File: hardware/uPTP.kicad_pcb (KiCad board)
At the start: 4 copper layers, 40 x 50 mm, 78 parts, among them J1 PPS_UFL, J2 PPS_SMA, J3 LED, J4 UART_HDR, J5 HC-RJ45-055-7, J6 AUX_PWR, J7 PROG, U1 XC6206P332MR-G, U2 SI3404-A-GMR, U3 CH32V307WCU6, X1 X50328MSB2GI

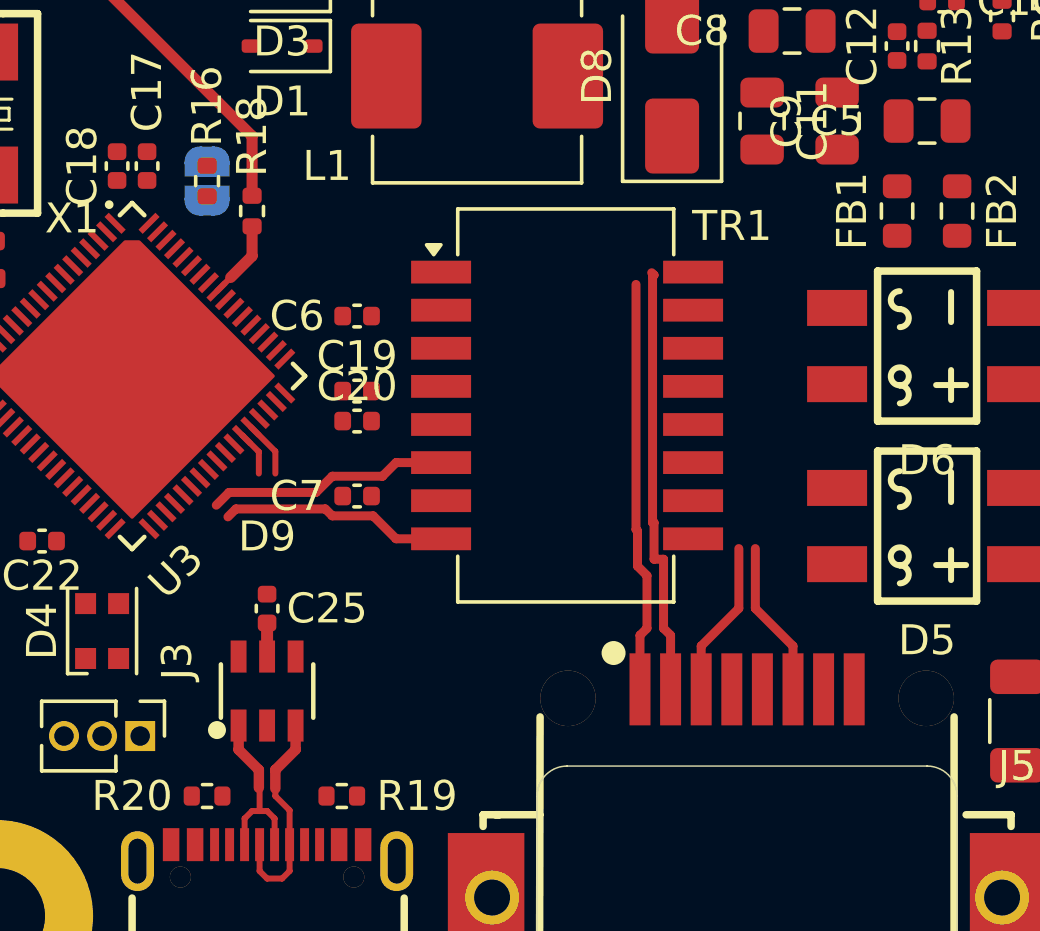
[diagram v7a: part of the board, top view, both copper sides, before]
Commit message: Change pin layout to make Ethernet Routing nicer
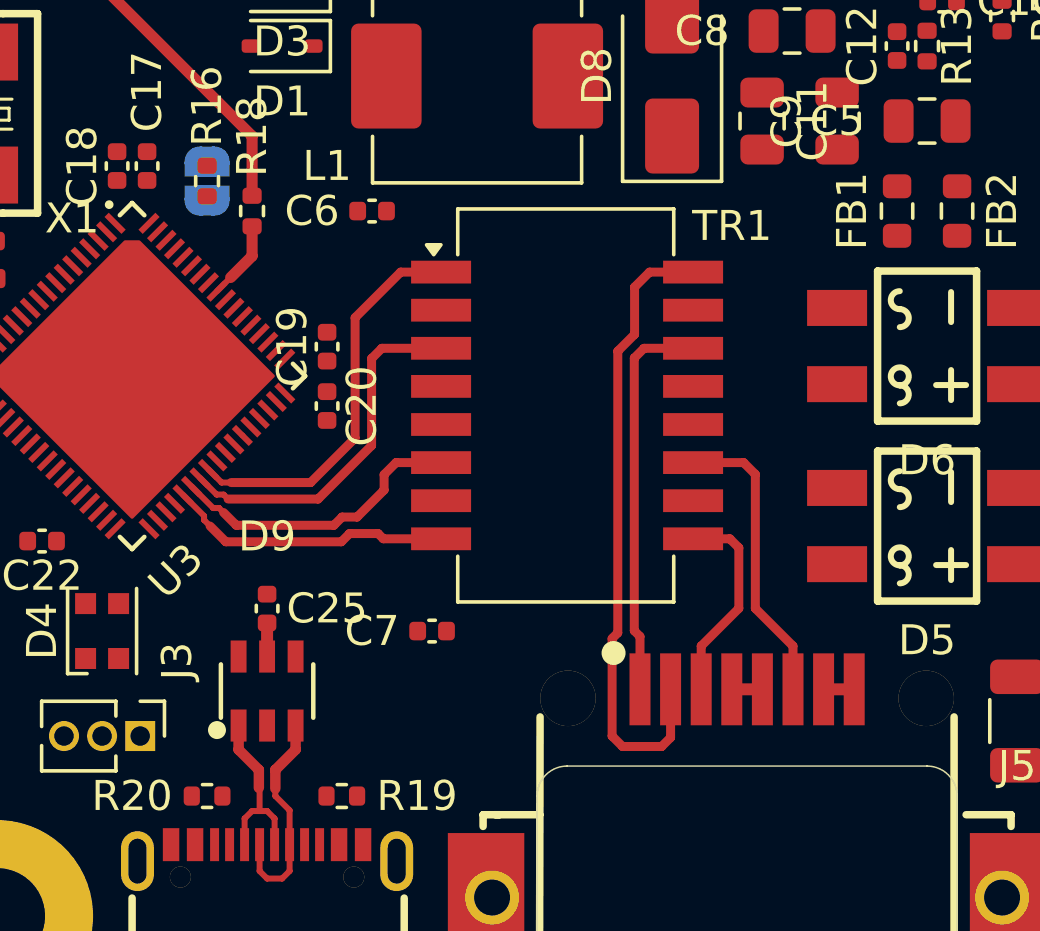
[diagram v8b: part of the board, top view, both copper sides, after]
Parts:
- moved C7 5.15 mm to (148.5, 111.5)
- moved C6 3.54 mm to (146.5, 97.5)
- moved C19 1.79 mm to (145.0, 102.0), turned to 90 degrees
- moved C20 1.12 mm to (145.0, 104.0), turned to -90 degrees
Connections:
- TR1 pad 1: /Ethernet and POE/ETH_D_TX_P -> /Ethernet and POE/ETH_D_TX_N
- TR1 pad 11: /Ethernet and POE/ETH_D_ISO_RX_P -> /Ethernet and POE/ETH_D_ISO_RX_N
- TR1 pad 14: /Ethernet and POE/ETH_D_ISO_TX_N -> /Ethernet and POE/ETH_D_ISO_TX_P
- TR1 pad 16: /Ethernet and POE/ETH_D_ISO_TX_P -> /Ethernet and POE/ETH_D_ISO_TX_N
- TR1 pad 3: /Ethernet and POE/ETH_D_TX_N -> /Ethernet and POE/ETH_D_TX_P
- TR1 pad 6: /Ethernet and POE/ETH_D_RX_P -> /Ethernet and POE/ETH_D_RX_N
- TR1 pad 8: /Ethernet and POE/ETH_D_RX_N -> /Ethernet and POE/ETH_D_RX_P
- TR1 pad 9: /Ethernet and POE/ETH_D_ISO_RX_N -> /Ethernet and POE/ETH_D_ISO_RX_P
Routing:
- net /Ethernet and POE/ETH_D_TX_N: track 0.00 -> 13.2 mm
- net /Ethernet and POE/ETH_D_TX_P: track 0.00 -> 12.1 mm
- net /Ethernet and POE/ETH_D_ISO_TX_N: track 14.4 -> 21.3 mm
- net /Ethernet and POE/ETH_D_ISO_RX_N: track 5.21 -> 9.92 mm
- net /Ethernet and POE/ETH_D_RX_N: track 7.63 -> 10.0 mm
- net /MCU/USB_D_N: track 1.89 -> 0.00 mm
- net /Ethernet and POE/ETH_D_ISO_RX_P: track 5.21 -> 6.89 mm
- net /MCU/USB_D_P: track 1.50 -> 0.00 mm
- net /Ethernet and POE/ETH_D_RX_P: track 8.08 -> 9.52 mm
- net /Ethernet and POE/ETH_TX2: track 0.00 -> 1.02 mm
- net /Ethernet and POE/ETH_RX2: track 0.00 -> 1.02 mm
- net /Ethernet and POE/ETH_D_ISO_TX_P: track 13.7 -> 13.2 mm
